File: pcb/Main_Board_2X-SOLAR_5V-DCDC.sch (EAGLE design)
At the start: 74 parts, among them CN5 USBA_FEMALE, IC1 MCP73871, IC2 MCP73871, T2 MMUN2133LT1G, U3 TPS61090RSAR

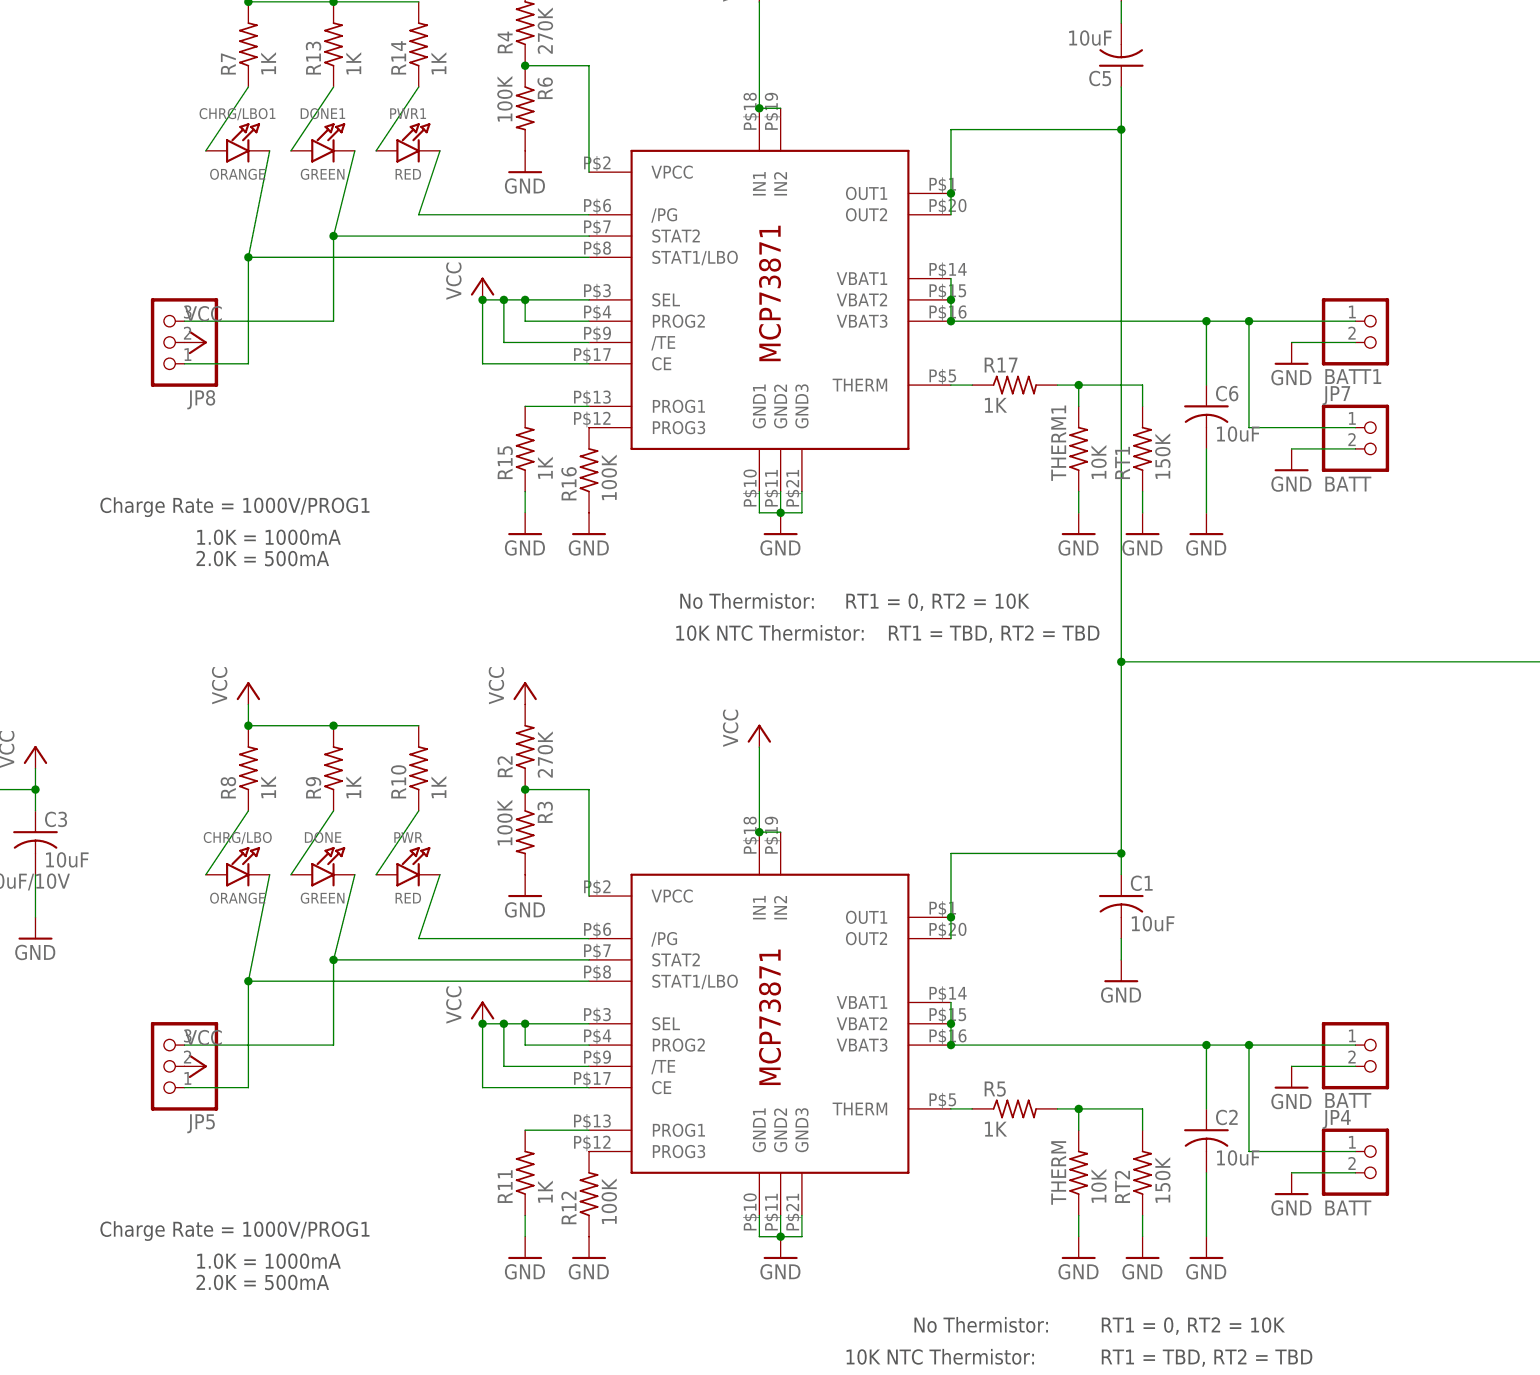
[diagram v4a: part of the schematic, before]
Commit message: Part removal and gitignore update
removed more jumpers and headers and updated the ignore file to ignore autosave files
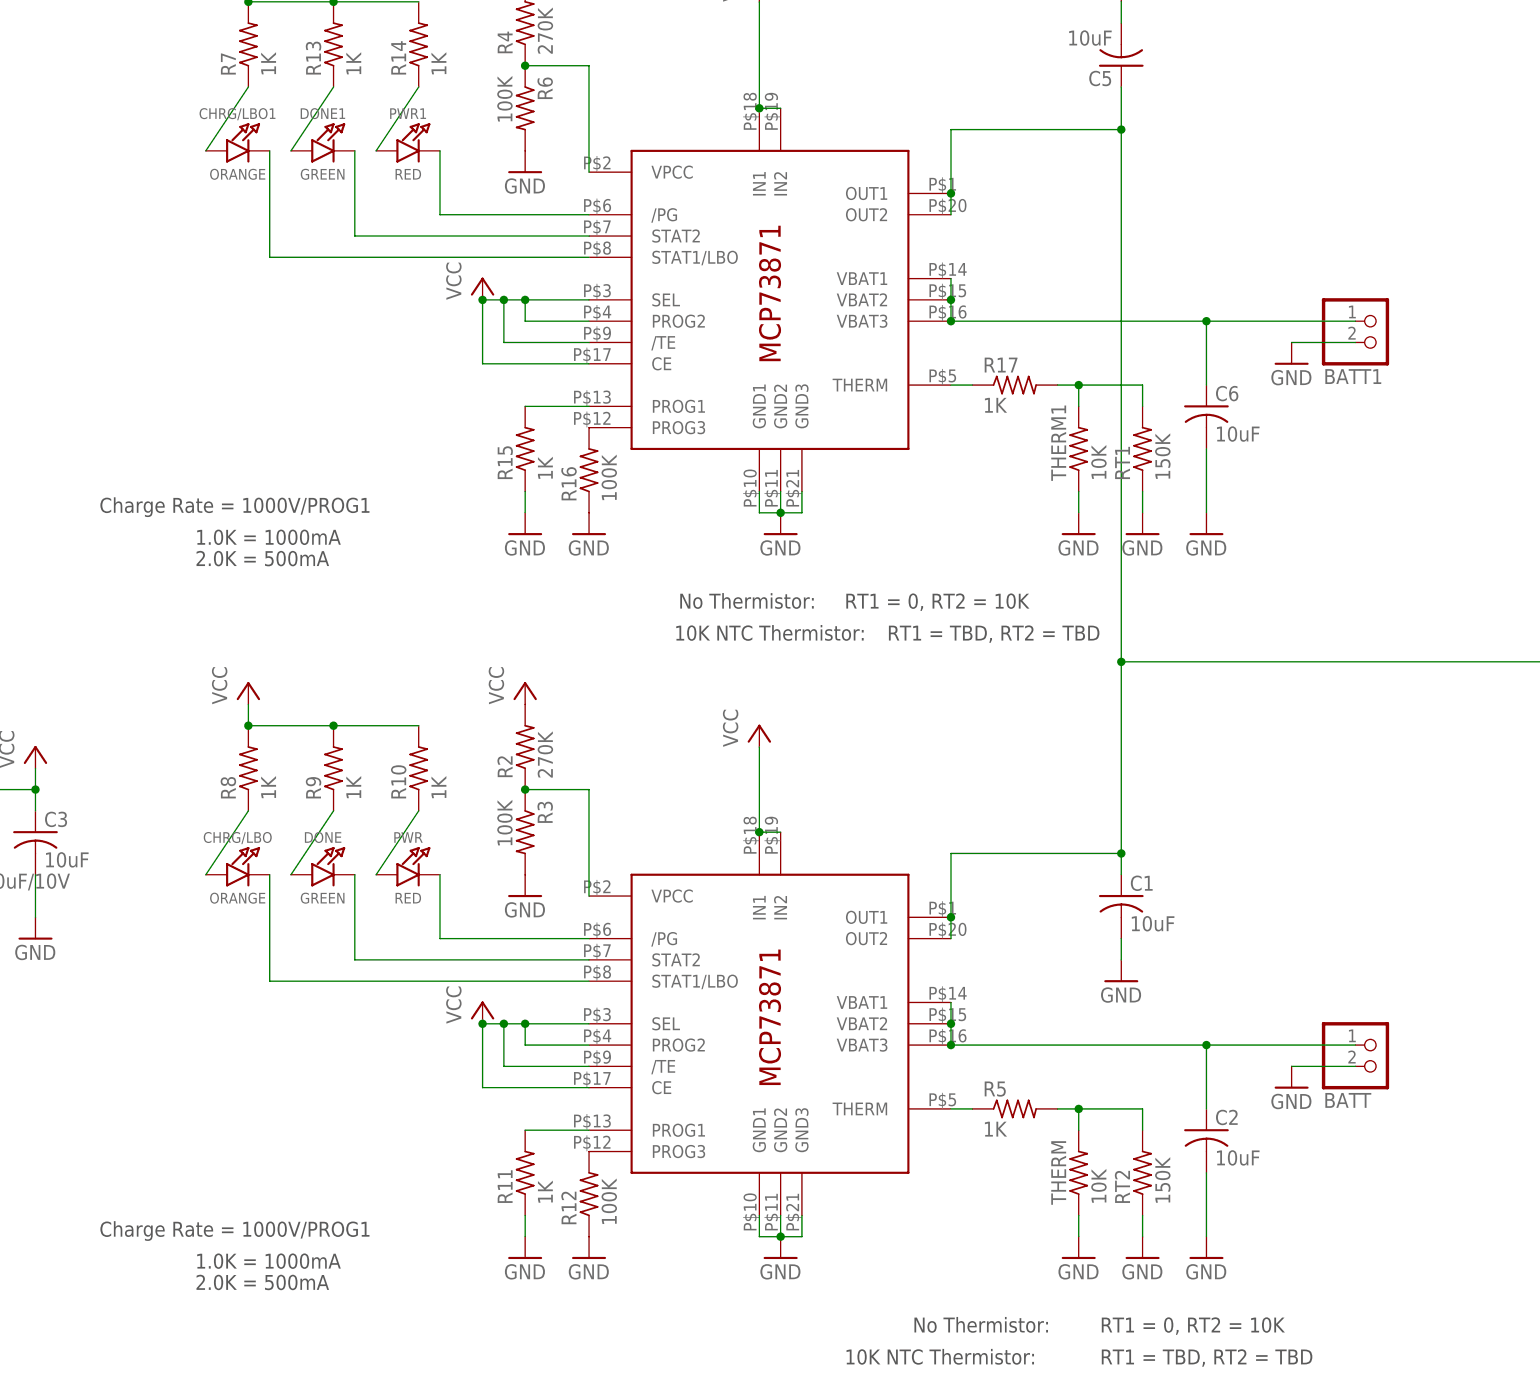
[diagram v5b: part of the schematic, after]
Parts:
- removed JP4, JP7: BATT, microbuilder:HEADER-1X2ROUND
- removed JP5, JP8: (no value), adafruit:PINHD-1X3CB
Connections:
- net BATT: no longer JP4.1
- net BATT1: no longer JP7.1
- net GND: no longer JP4.2, JP7.2
- net N$11: no longer JP5.1
- net N$17: no longer JP8.3
- net N$18: no longer JP8.1
- net N$4: no longer JP5.3
- net VCC: no longer JP5.2, JP8.2

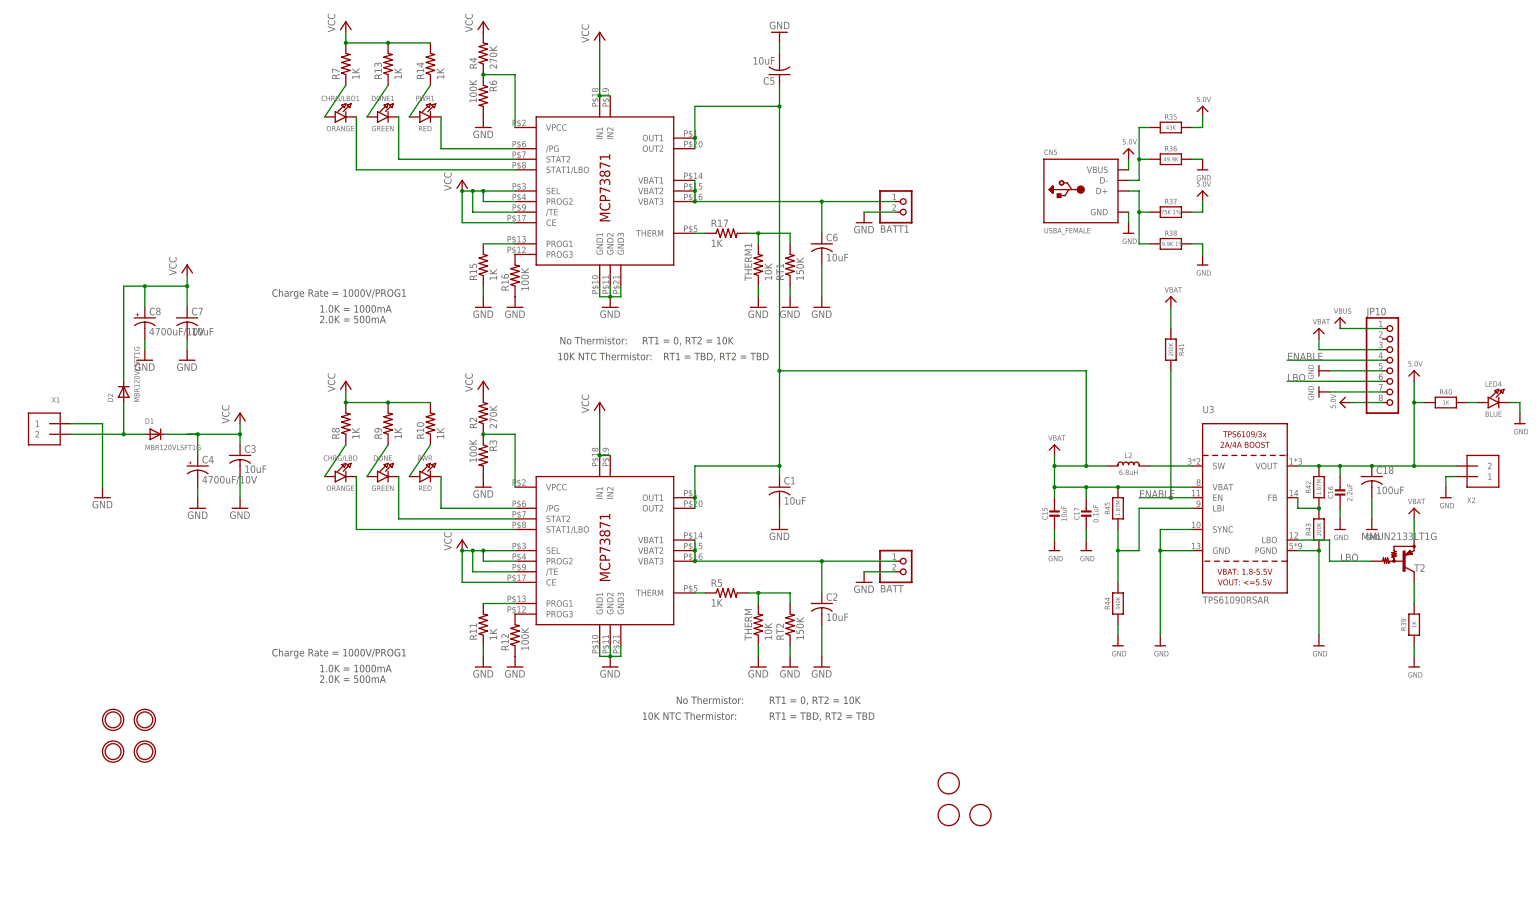
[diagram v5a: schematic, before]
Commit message: Added jumpers and diodes to load line regulation
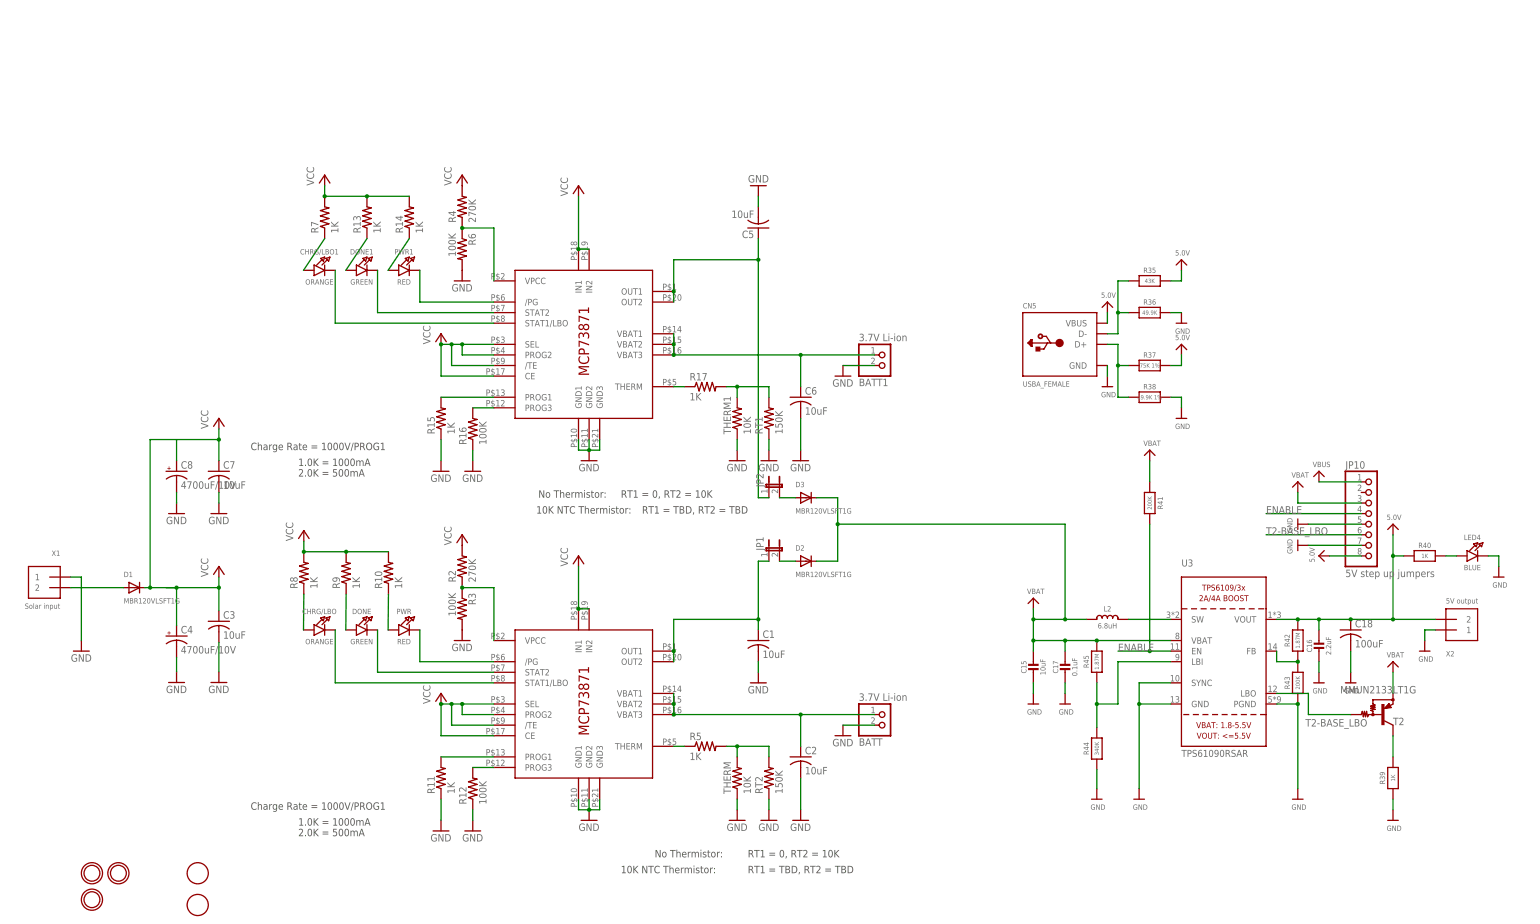
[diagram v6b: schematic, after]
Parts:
- removed U$2: FIDUCIAL, adafruit:FIDUCIAL
- removed U$5, U$7: MOUNTINGHOLE2.5, microbuilder:MOUNTINGHOLE2.5
- added D3: MBR120VLSFT1G, microbuilder:DIODESOD-123
- added JP1, JP2: (no value), jumper:JP1E
- added U$1: MOUNTINGHOLE2.5, microbuilder:MOUNTINGHOLE2.5
- BATT, BATT1: value (none) -> 3.7V Li-ion
- JP10: value (none) -> 5V step up jumpers
- X1: value (none) -> Solar input
- X2: value (none) -> 5V output
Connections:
- net LBO renamed T2-BASE_LBO
- net N$1 renamed PG
- net N$11 renamed STAT1
- net N$15 renamed PROG3
- net N$16 renamed PROG1
- net N$17 renamed STAT2_1
- net N$18 renamed STAT1_1
- net N$22 renamed PROG3_1
- net N$23 renamed PROG1_1
- net N$26 renamed T2-DRAIN
- net N$4 renamed STAT2
- net N$9 renamed PG_1
- new net N$1: D3.A, JP2.2
- new net N$2: D2.A, JP1.2
- new net VOUT: C1.1, IC1.OUT1, IC1.OUT2, JP1.1
- new net VOUT1: C5.1, IC2.OUT1, IC2.OUT2, JP2.1
- net PV_IN: no longer D2.A
- net VBAT: now also D2.C, D3.C; no longer C1.1, C5.1, IC1.OUT1, IC1.OUT2, IC2.OUT1, IC2.OUT2
- net VCC: no longer D2.C
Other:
- moved on the sheet: BATT, BATT1, C1, C15, C16, C17, C18, C2, C3, C4, C5, C6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

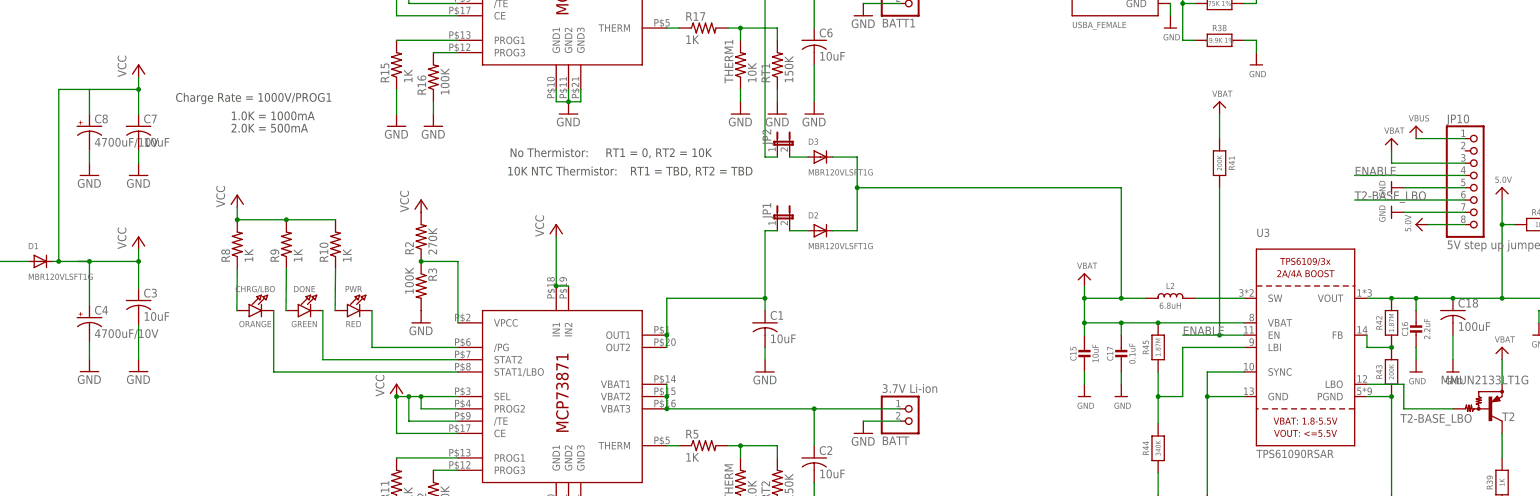
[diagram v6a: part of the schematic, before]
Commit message: Cleaned up silkscreen
Moved silkscreen for better visibility during assembly and deleted extra labels. Shrank board a little bit smaller in dimension
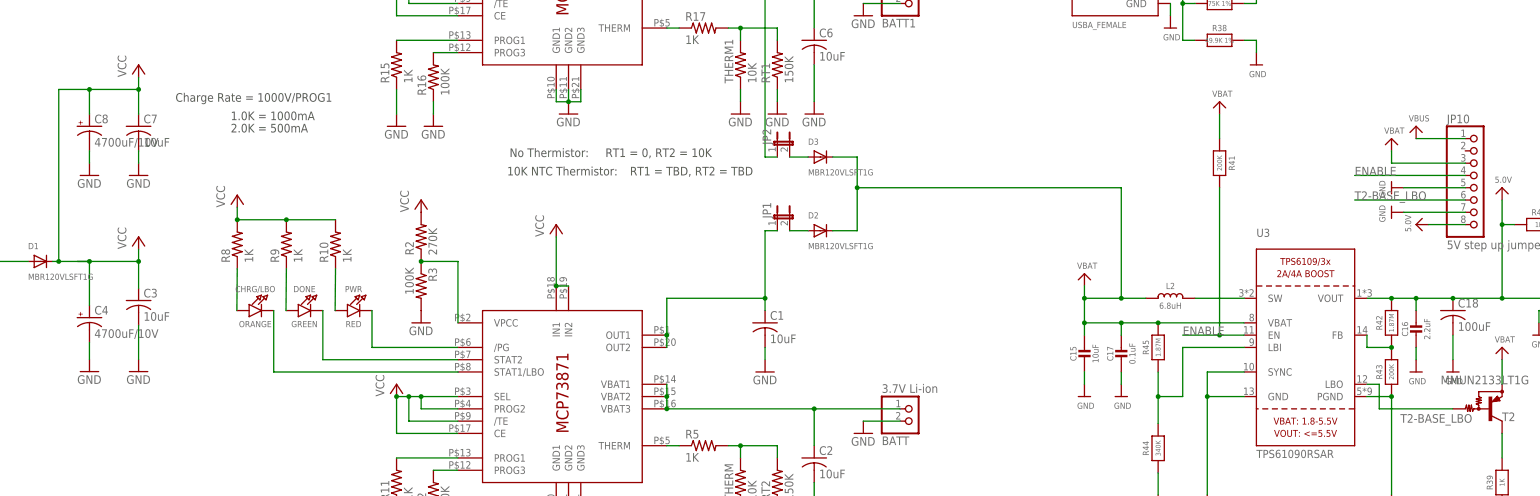
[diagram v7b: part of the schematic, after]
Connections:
- net N$1 renamed DIODE_PROT_1
- net N$2 renamed DIODE_PROT
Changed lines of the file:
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@@
 <setting verticaltext="up"/>
 </settings>
-<grid distance="50" unitdist="mil" unit="mil" style="lines" multiple="1" display="no" altdistance="5" altunitdist="mil" altunit="mil"/>
+<grid distance="0.1" unitdist="inch" unit="inch" style="lines" multiple="1" display="no" altdistance="0.01" altunitdist="inch" altunit="inch"/>
 <layers>
 <layer number="1" name="Top" color="4" fill="1" visible="no" active="no"/>
@@
 <wire x1="34.29" y1="115.57" x2="34.29" y2="80.01" width="0.1524" layer="91"/>
 <junction x="34.29" y="80.01"/>
+<junction x="40.64" y="115.57"/>
 </segment>
 </net>
@@
 <segment>
 <pinref part="U3" gate="G$1" pin="LBO"/>
-<wire x1="304.8" y1="54.61" x2="312.42" y2="54.61" width="0.1524" layer="91"/>
-<wire x1="312.42" y1="54.61" x2="312.42" y2="49.53" width="0.1524" layer="91"/>
-<wire x1="312.42" y1="49.53" x2="322.58" y2="49.53" width="0.1524" layer="91"/>
+<wire x1="304.8" y1="54.61" x2="307.34" y2="54.61" width="0.1524" layer="91"/>
+<wire x1="307.34" y1="54.61" x2="307.34" y2="49.53" width="0.1524" layer="91"/>
+<wire x1="307.34" y1="49.53" x2="322.58" y2="49.53" width="0.1524" layer="91"/>
 <pinref part="T2" gate="G$1" pin="B"/>
 <label x="311.71" y="46.655" size="1.778" layer="95"/>
@@
 </segment>
 </net>
-<net name="N$1" class="0">
+<net name="DIODE_PROT_1" class="0">
 <segment>
 <pinref part="D3" gate="G$1" pin="A"/>
@@
 </segment>
 </net>
-<net name="N$2" class="0">
+<net name="DIODE_PROT" class="0">
 <segment>
 <pinref part="D2" gate="G$1" pin="A"/>
